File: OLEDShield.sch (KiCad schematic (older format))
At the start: 15 parts, among them P1 CONN_5X2, P2 CONN_5X2, P3 CONN_1, P4 CONN_1, P5 CONN_1

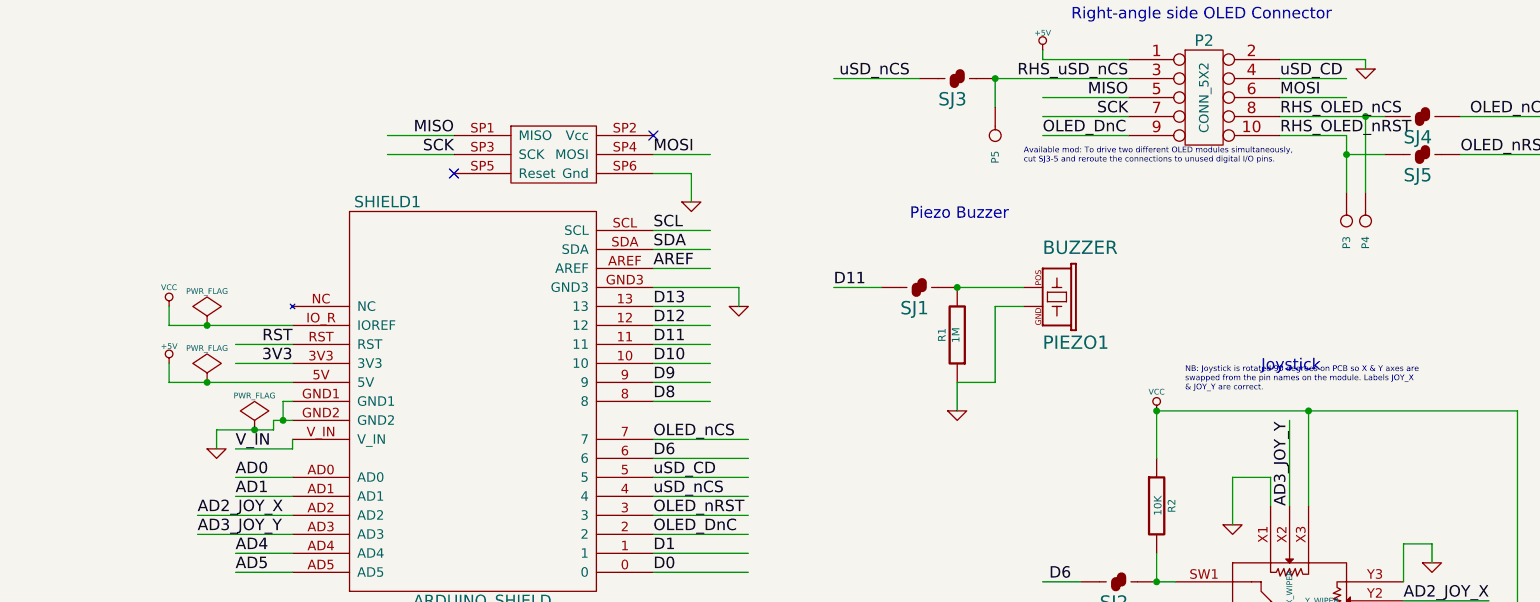
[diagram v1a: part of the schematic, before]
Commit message: Add ground pour in prototyping area, fix board edges to clear Ethernet jack, finish silkscreening
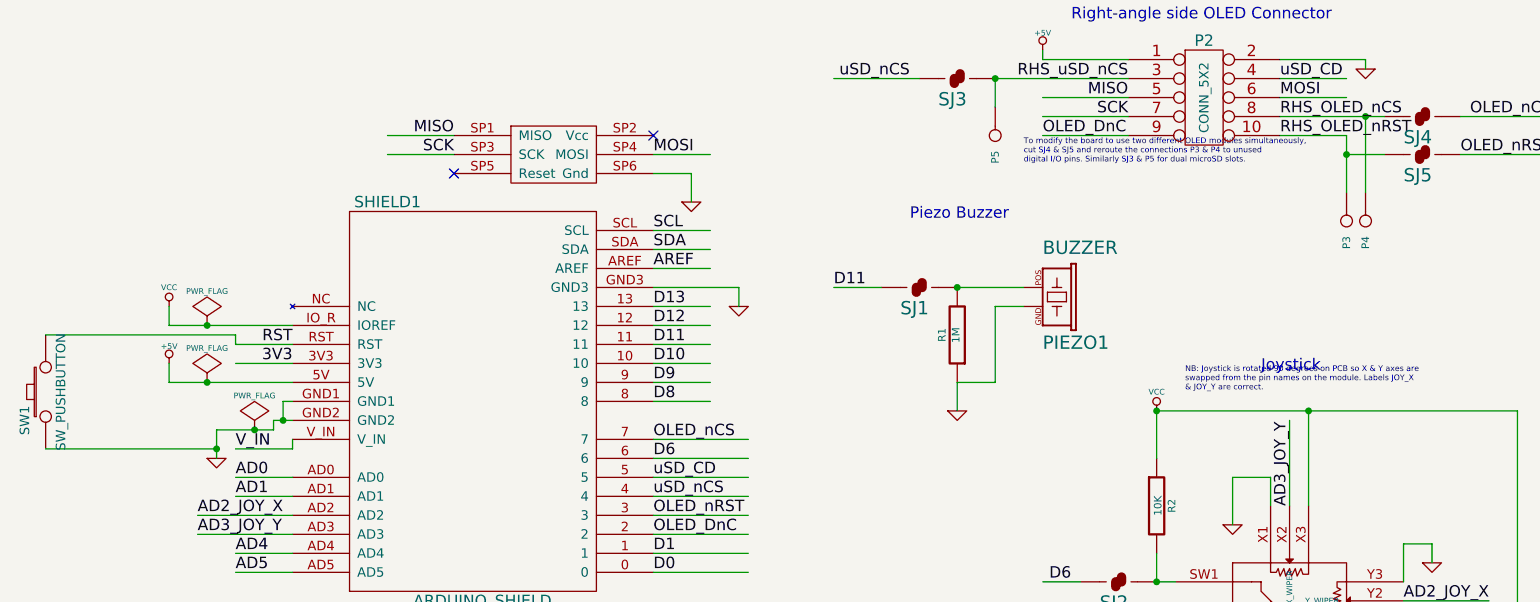
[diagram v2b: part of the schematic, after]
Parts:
- added SW1: SW_PUSHBUTTON, ~, symbol SW_PUSHBUTTON
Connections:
- wire segments 100 -> 103
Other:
- note added: "To modify the board to use two different OLED modules simultaneously,\ncut SJ4 & SJ5 and reroute the connections P3 & P4 to unused\ndigital I/O pins. Similarly SJ3 & P5 for dual microSD slots."
- note removed: "Available mod: To drive two different OLED modules simultaneously,\ncut SJ3-5 and reroute the connections to unused digital I/O pins."
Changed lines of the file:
@@
-EESchema Schematic File Version 2  date Mon 10 Jun 2013 15:39:52 EST
+EESchema Schematic File Version 2  date Wed 12 Jun 2013 13:40:15 EST
 LIBS:freetronics_kicad_sch_lib
 LIBS:power
@@
 Sheet 1 1
 Title "Freetronics OLEDShield              http://www.freetronics.com/oledshield"
-Date "31 may 2013"
-Rev "1.0"
+Date "12 jun 2013"
+Rev "0.1"
 Comp "(C)2013 Freetronics Pty Ltd"
 Comment1 "Released under TAPR Open Hardware License www.tapr.org/ohl"
@@
 L GND #PWR04
 U 1 1 51A408D4
-P 4100 5400
-F 0 "#PWR04" H 4100 5400 30  0001 C CNN
-F 1 "GND" H 4100 5330 30  0001 C CNN
-F 2 "" H 4100 5400 60  0000 C CNN
-F 3 "" H 4100 5400 60  0000 C CNN
-	1    4100 5400
+P 4100 5450
+F 0 "#PWR04" H 4100 5450 30  0001 C CNN
+F 1 "GND" H 4100 5380 30  0001 C CNN
+F 2 "" H 4100 5450 60  0000 C CNN
+F 3 "" H 4100 5450 60  0000 C CNN
+	1    4100 5450
 	1    0    0    -1
 $EndComp
@@
 	3850 5050 3850 4950
 Wire Wire Line
-	4100 5400 4100 5300
+	4100 5300 4100 5450
 Wire Wire Line
 	3850 4750 3850 4650
@@
 	10650 3850 11150 3850
 Text Notes 8350 3900 0    30   ~ 0
-Available mod: To drive two different OLED modules simultaneously,\ncut SJ3-5 and reroute the connections to unused digital I/O pins.
+To modify the board to use two different OLED modules simultaneously,\ncut SJ4 & SJ5 and reroute the connections P3 & P4 to unused\ndigital I/O pins. Similarly SJ3 & P5 for dual microSD slots.
 Wire Wire Line
 	10350 6100 10350 5900
@@
 Text Label 8900 3450 2    60   ~ 0
 RHS_uSD_nCS
+$Comp
+L SW_PUSHBUTTON SW1
+U 1 1 51B7C154
+P 3200 5100
+F 0 "SW1" H 3050 5210 50  0000 C CNN
+F 1 "SW_PUSHBUTTON" H 3200 5020 50  0000 C CNN
+F 2 "~" H 3200 5100 60  0000 C CNN
+F 3 "~" H 3200 5100 60  0000 C CNN
+	1    3200 5100
+	0    -1   -1   0
+$EndComp
+Wire Wire Line
+	4200 4800 4200 4850
+Wire Wire Line
+	3200 4800 4200 4800
+Wire Wire Line
+	3200 5400 4100 5400
+Connection ~ 4100 5400
 $EndSCHEMATC

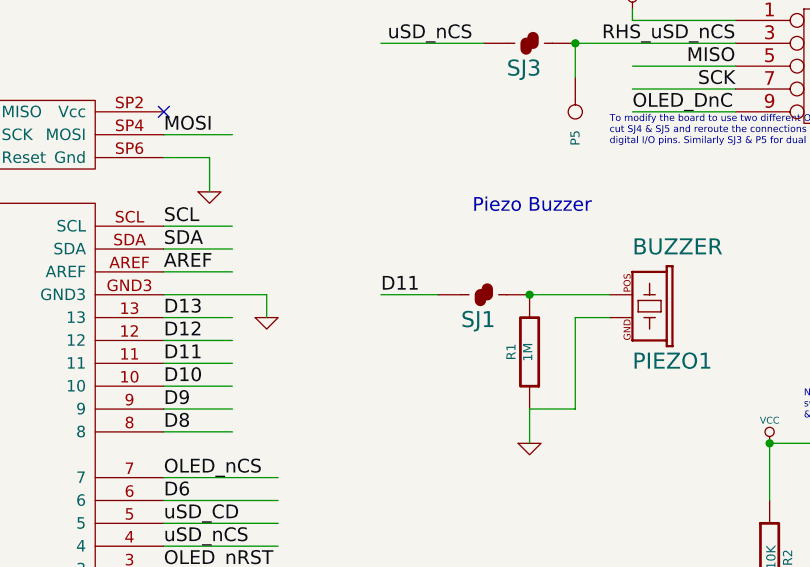
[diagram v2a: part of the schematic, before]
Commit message: Move piezo from D11 to D9
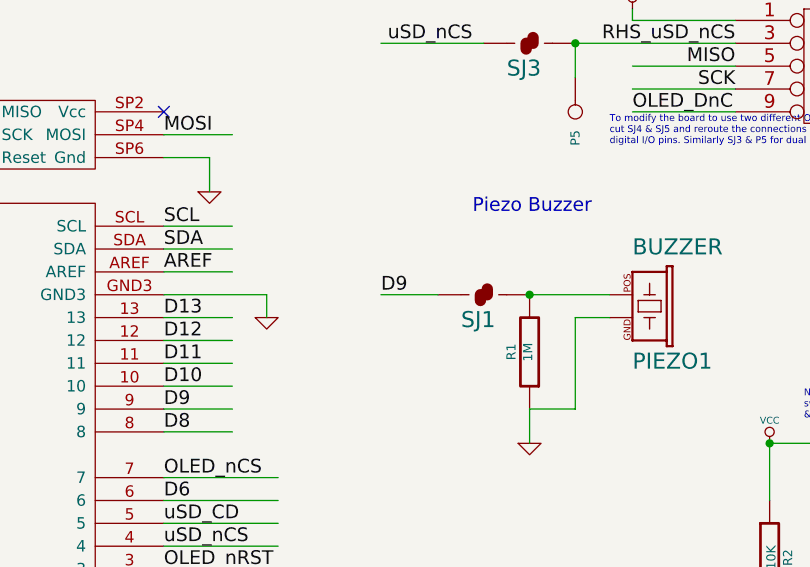
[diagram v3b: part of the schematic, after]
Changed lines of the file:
@@
-EESchema Schematic File Version 2  date Wed 12 Jun 2013 13:40:15 EST
+EESchema Schematic File Version 2  date Thu 18 Jul 2013 12:36:17 EST
 LIBS:freetronics_kicad_sch_lib
 LIBS:power
@@
 Sheet 1 1
 Title "Freetronics OLEDShield              http://www.freetronics.com/oledshield"
-Date "12 jun 2013"
+Date "18 jul 2013"
 Rev "0.1"
 Comp "(C)2013 Freetronics Pty Ltd"
@@
 $EndComp
 Text Label 7350 4550 0    60   ~ 0
-D11
+D9
 Text Label 6400 4850 0    60   ~ 0
 D11

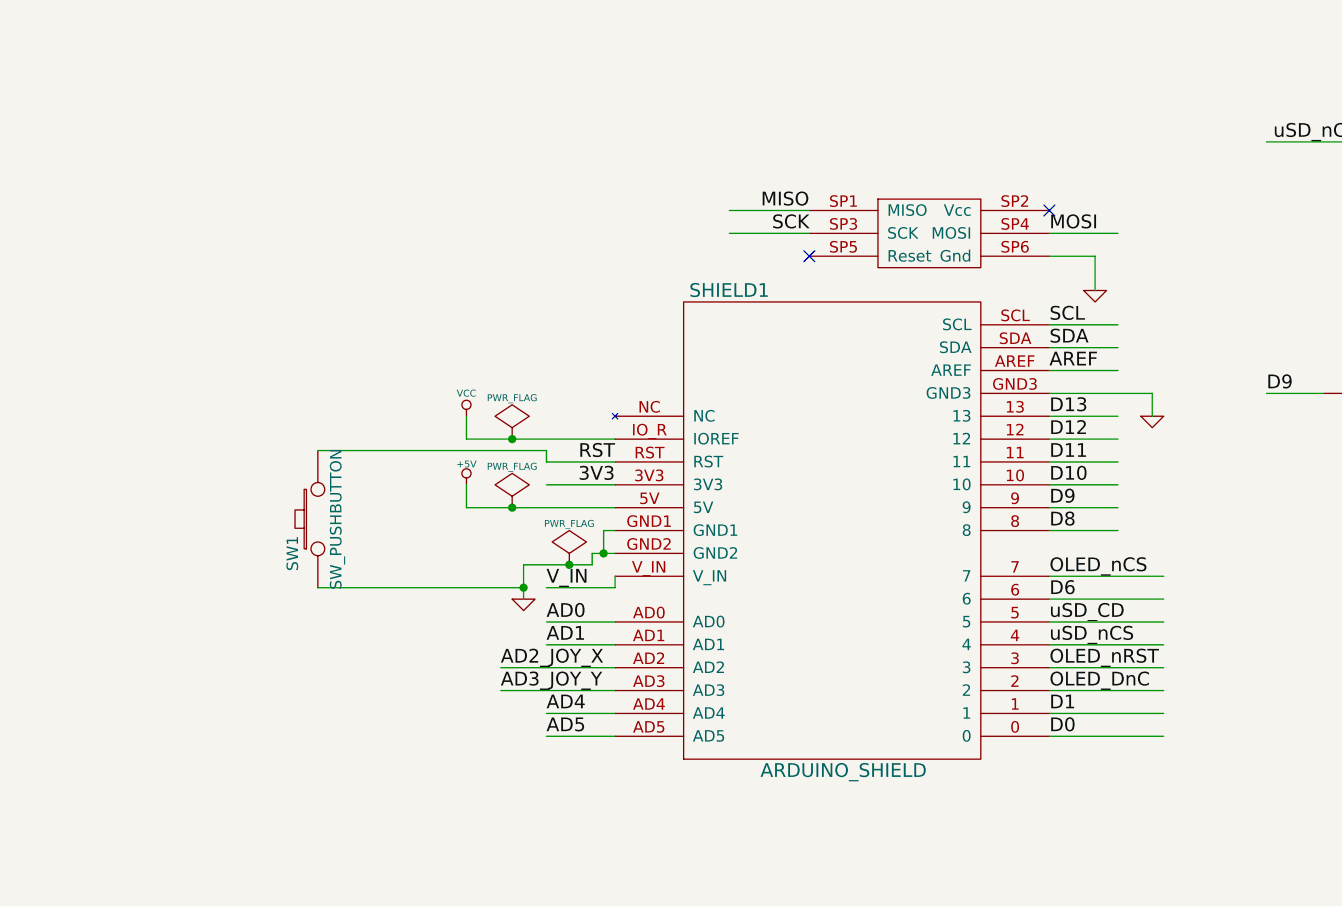
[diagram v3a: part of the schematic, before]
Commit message: Clean up silkscreen positioning, label formatting
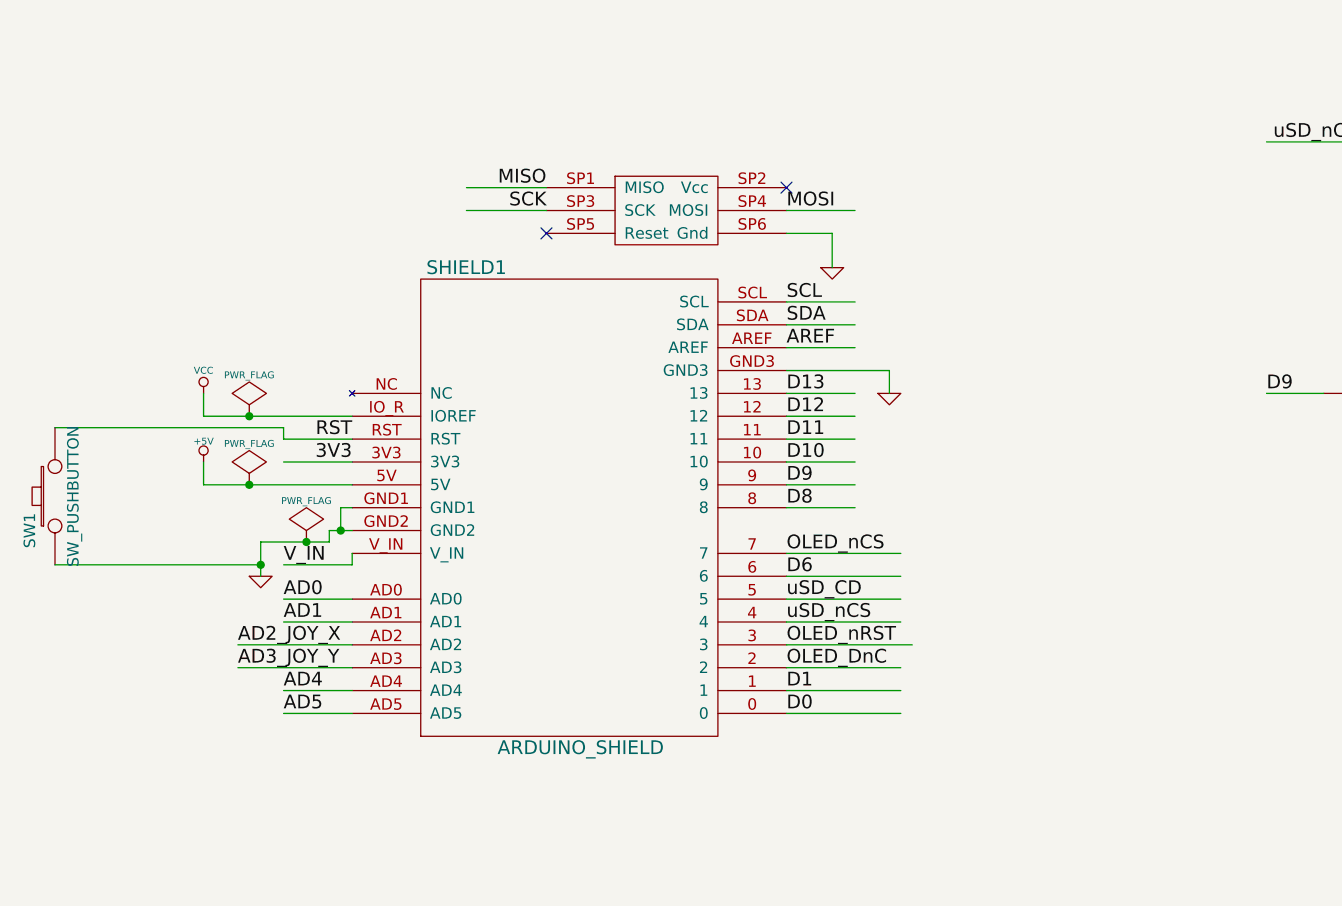
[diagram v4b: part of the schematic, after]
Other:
- moved on the sheet: SHIELD1, SW1

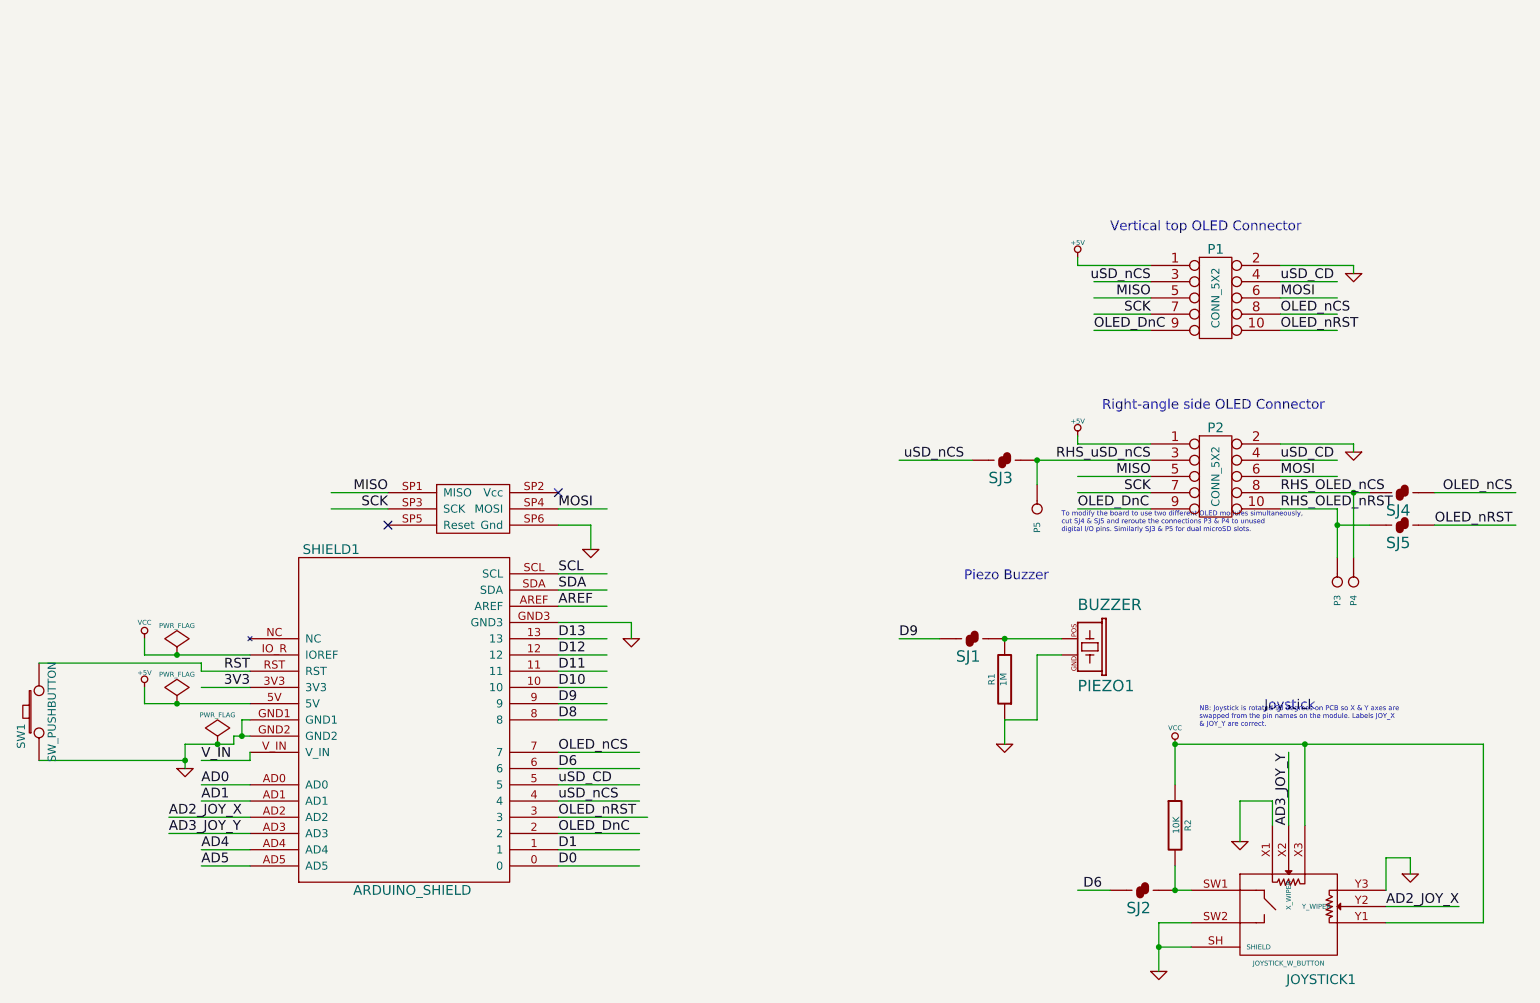
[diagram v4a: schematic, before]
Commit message: Add pulldown on nRST to hold OLED in reset during board reset
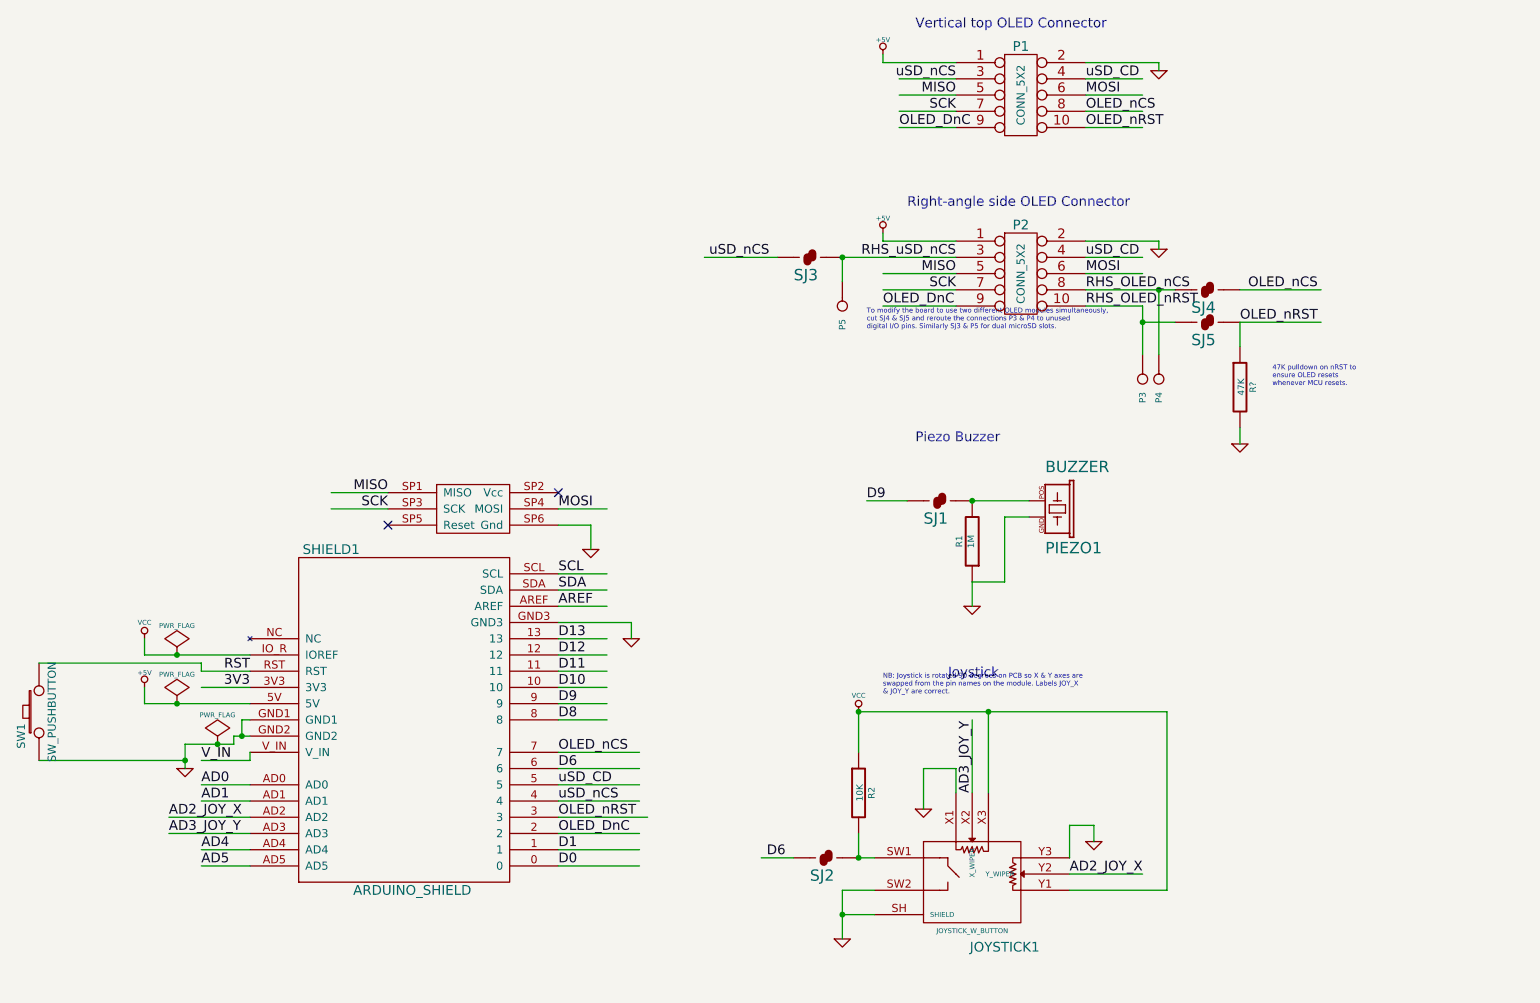
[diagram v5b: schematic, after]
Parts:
- added R?: 47K, symbol R
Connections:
- wire segments 103 -> 105
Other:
- note added: "47K pulldown on nRST to\nensure OLED resets\nwhenever MCU resets."
- moved on the sheet: JOYSTICK1, P1, P2, P3, P4, P5, PIEZO1, R1, R2, SJ1, SJ2, SJ3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

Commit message: More minor cosmetic cleanup, bump revision to 1.1
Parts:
- gave numbers to parts that had none: 1
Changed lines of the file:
@@
 Sheet 1 1
 Title "Freetronics OLEDShield              http://www.freetronics.com/oledshield"
-Date "19 jul 2013"
-Rev "0.1"
+Date "24 Jul 2013"
+Rev "1.1"
 Comp "(C)2013 Freetronics Pty Ltd"
 Comment1 "Released under TAPR Open Hardware License www.tapr.org/ohl"
@@
 	3050 4700 2050 4700
 $Comp
-L R R?
+L R R3
 U 1 1 51EF193C
 P 9450 3000
-F 0 "R?" V 9530 3000 40  0000 C CNN
+F 0 "R3" V 9530 3000 40  0000 C CNN
 F 1 "47K" V 9457 3001 40  0000 C CNN
 F 2 "" V 9380 3000 30  0000 C CNN
@@
 	9450 2750 9450 2600
 $Comp
-L GND #PWR?
+L GND #PWR018
 U 1 1 51EF19C5
 P 9450 3350
-F 0 "#PWR?" H 9450 3350 30  0001 C CNN
+F 0 "#PWR018" H 9450 3350 30  0001 C CNN
 F 1 "GND" H 9450 3280 30  0001 C CNN
 F 2 "" H 9450 3350 60  0000 C CNN

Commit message: Mild cleanup for 1.2 - deepen cutout for Ethernet models, add NC breakout hole, tidy up, swap X axis polarity
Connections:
- wire segments 105 -> 104
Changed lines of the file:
@@
 L GND #PWR02
 U 1 1 51A407AD
-P 8550 5800
-F 0 "#PWR02" H 8550 5800 30  0001 C CNN
-F 1 "GND" H 8550 5730 30  0001 C CNN
-F 2 "" H 8550 5800 60  0000 C CNN
-F 3 "" H 8550 5800 60  0000 C CNN
-	1    8550 5800
+P 8550 6200
+F 0 "#PWR02" H 8550 6200 30  0001 C CNN
+F 1 "GND" H 8550 6130 30  0001 C CNN
+F 2 "" H 8550 6200 60  0000 C CNN
+F 3 "" H 8550 6200 60  0000 C CNN
+	1    8550 6200
 	1    0    0    -1
 $EndComp
@@
 Connection ~ 7000 6250
 Wire Wire Line
-	8400 6100 9000 6100
-Wire Wire Line
 	5250 4450 5700 4450
 Wire Wire Line
@@
 	9450 2600 9950 2600
 Wire Wire Line
-	8400 5900 8400 5700
-Wire Wire Line
-	8400 5700 8550 5700
-Wire Wire Line
-	8550 5700 8550 5800
+	8400 6100 8550 6100
+Wire Wire Line
+	8550 6100 8550 6200
 Wire Wire Line
 	5250 4150 5550 4150
@@
 Wire Wire Line
 	3050 4750 3350 4750
-Wire Wire Line
-	9000 5000 9000 6100
 Wire Wire Line
 	5700 4450 5700 4550
@@
 Text Notes 9650 3000 0    30   ~ 0
 47K pulldown on nRST to\nensure OLED resets\nwhenever MCU resets.
+Wire Wire Line
+	8400 5900 9000 5900
+Wire Wire Line
+	9000 5900 9000 5000
 $EndSCHEMATC
